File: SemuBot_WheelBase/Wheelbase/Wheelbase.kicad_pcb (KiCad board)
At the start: 2 copper layers, 110 x 90 mm, 136 parts, among them IC1 DRV8353FSRTAR, IC2 DRV8353FSRTAR, IC3 DRV8353FSRTAR, IC4 ADS131M03IRUKT, IC5 ADS131M03IRUKT, IC6 ADS131M03IRUKT, J1 10155435-00011LF, J10 B5B-XH-A_LF__SN_, J11 B5B-XH-A_LF__SN_, J12 B5B-XH-A_LF__SN_, J13 MTSW-104-09-L-S-400, J14 XT30PW-M, J15 MTSW-104-09-L-S-400, J2 MTSW-102-09-L-S-400, J3 MR30PW-M, J4 B5B-XH-A_LF__SN_, J5 B5B-XH-A_LF__SN_, J6 B5B-XH-A_LF__SN_, J7 MR30PW-M, J8 MR30PW-M, J9 DS1013-10SSIB1, Q1 AON7262E, Q10 AON7262E, Q11 AON7262E, Q12 AON7262E, Q13 AON7262E, Q14 AON7262E, Q15 AON7262E, Q19 AON7262E, Q2 AON7262E, Q20 AON7262E, Q21 AON7262E, Q3 AON7262E, Q4 AON7262E, Q5 AON7262E, Q6 AON7262E, Q7 AON7262E, Q8 AON7262E, Q9 AON7262E, U1 STM32F303RET6, U5 RT9013-33GB, Y1 ECS-2520MVLC-081.92-CN-TR, Y2 X322516MLB4SI

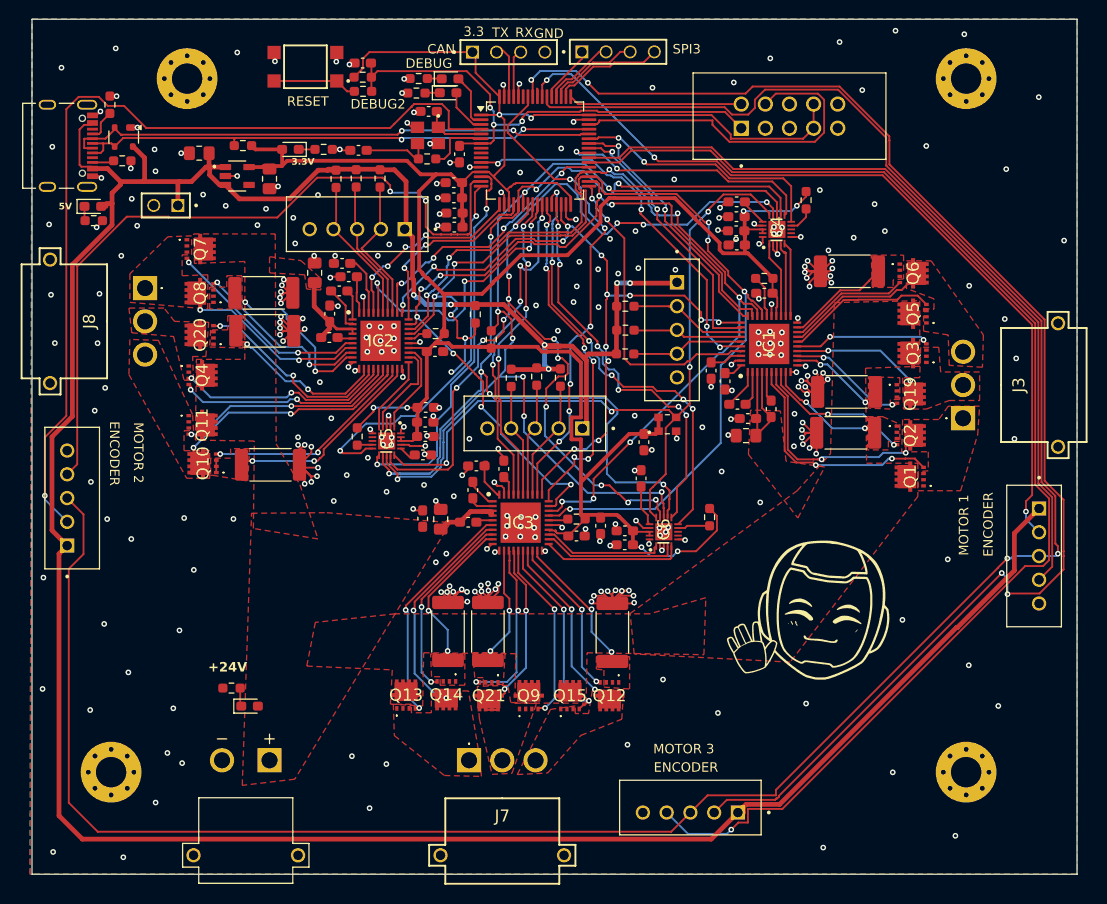
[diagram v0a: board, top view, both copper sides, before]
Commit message: New 4-layer board
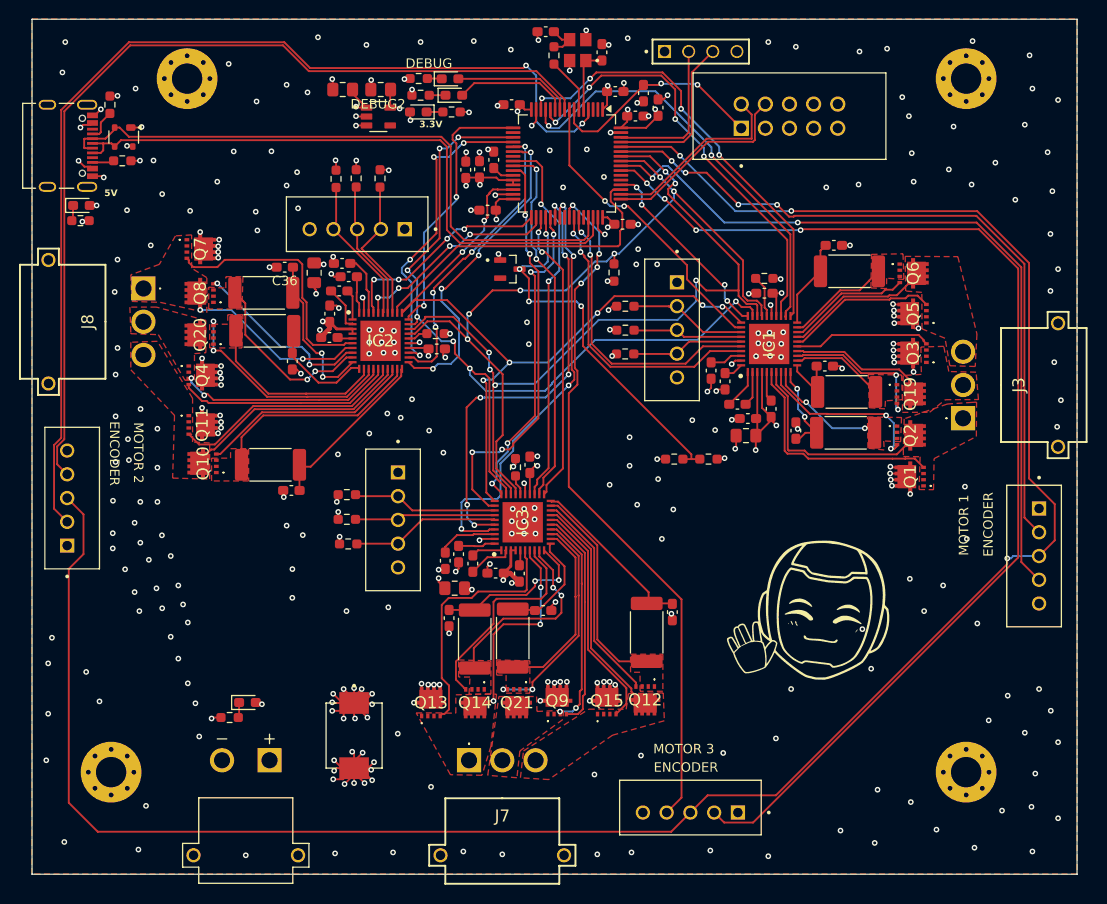
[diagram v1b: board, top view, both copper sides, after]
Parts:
- removed C2, C50, C51, C52, C53: 100nF, Capacitor_SMD:C_0603_1608Metric_Pad1.08x0.95mm_HandSolder
- removed C22: 220nF, Capacitor_SMD:C_0603_1608Metric_Pad1.08x0.95mm_HandSolder
- removed IC4, IC5, IC6: ADS131M03IRUKT, ADS131M:QFN40P300X300X80-21N-D
- removed J15: MTSW-104-09-L-S-400, MTSW-104-09-L-S-400:SAMTEC_MTSW-104-09-L-S-400
- removed J2: MTSW-102-09-L-S-400, MTSW-102-09-L-S-400.:SAMTEC_MTSW-102-09-L-S-400
- removed R21, R22, R3: 1.5K, Resistor_SMD:R_0603_1608Metric_Pad0.98x0.95mm_HandSolder
- removed R23: 10k, Resistor_SMD:R_0603_1608Metric_Pad0.98x0.95mm_HandSolder
- removed R24: 100, Resistor_SMD:R_0603_1608Metric_Pad0.98x0.95mm_HandSolder
- removed R36: 1.5k, Resistor_SMD:R_0603_1608Metric_Pad0.98x0.95mm_HandSolder
- removed S1: SWT0211-050010GSA_REVA, switch:SW_SWT0211-050010GSA_REVA
- removed Y1: ECS-2520MVLC-081.92-CN-TR, ECS-2520:OSC_ECS-2520MVLC-081.92-CN-TR
- added C41: 1uF 63V, Capacitor_SMD:C_0603_1608Metric_Pad1.08x0.95mm_HandSolder, F.Cu at (185.1, 97.3)
- added C42: 1uF 63V, Capacitor_SMD:C_0603_1608Metric_Pad1.08x0.95mm_HandSolder, F.Cu at (129.1, 96.8)
- added C43: 1uF 63V, Capacitor_SMD:C_0603_1608Metric_Pad1.08x0.95mm_HandSolder, F.Cu at (155.5, 123.0)
- added C44: 100nF, Capacitor_SMD:C_0603_1608Metric_Pad1.08x0.95mm_HandSolder, F.Cu at (165.2, 70.9)
- added C45: 100nF, Capacitor_SMD:C_0603_1608Metric_Pad1.08x0.95mm_HandSolder, F.Cu at (148.8, 76.5)
- added C46: 100nF, Capacitor_SMD:C_0603_1608Metric_Pad1.08x0.95mm_HandSolder, F.Cu at (147.3, 76.6)
- added D4: BZX84C3V3, BZX84C3V3:SOT95P240X115-3N, F.Cu at (152.0, 87.0)
- added D5: SMCJ33A, SMCJ33A:DIOM6859X262N, F.Cu at (135.6, 136.2)
- added R27: 10k, Resistor_SMD:R_0603_1608Metric_Pad0.98x0.95mm_HandSolder, F.Cu at (169.3, 107.0)
- C16, C34: value 220nF -> 100nF
- C35, C36, C37, C38, C39, C40: value 100nF -> 1uF 63V
- Q1, Q10, Q11, Q12, Q13, Q14, Q15, Q19, Q2, Q20, Q21, Q3, Q4, Q5, Q6, Q7, Q8, Q9: value AON7262E -> AONR62818
- R26: value 3.3K -> 91k
- U1: value STM32F303RET6 -> STM32G474RET6
- moved C34 36.9 mm to (150.3, 75.5), turned to 90 degrees
- moved R26 26.1 mm to (172.9, 107.0), turned to 180 degrees
- moved R31 25.6 mm to (134.8, 110.8), turned to 180 degrees
- moved R34 25.0 mm to (134.8, 113.4), turned to 180 degrees
- moved R38 24.5 mm to (135.0, 116.0), turned to 180 degrees
- moved C10 23.3 mm to (155.7, 62.1)
- moved C36 23.2 mm to (128.3, 86.8), turned to 180 degrees
- moved C35 20.5 mm to (182.1, 104.0), turned to 90 degrees
- moved C3 20.4 mm to (166.0, 68.5)
- moved J13 20.2 mm to (172.1, 64.2)
- moved C15 19.5 mm to (163.1, 68.4), turned to 0 degrees
- moved C11 19.3 mm to (161.7, 64.2), turned to 90 degrees
- moved C37 18.7 mm to (145.6, 123.8)
- moved Y2 18.1 mm to (159.1, 64.0), turned to 180 degrees
- moved J6 18.1 mm to (139.7, 113.5), turned to 90 degrees
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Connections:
- C16 pad 1: GND -> +3.3V
- C16 pad 2: Net-(IC4-CAP) -> GND
- C34 pad 1: GND -> Net-(U1-VSSA)
- C34 pad 2: Net-(IC6-CAP) -> GND
- C35 pad 1: +3.3V -> /Motor_1/SNA
- C36 pad 1: +3.3V -> /Motor_2/SNA
- C37 pad 1: +3.3V -> /Motor_3/SNA
- C38 pad 1: +3.3V -> /Motor_1/SNC
- C39 pad 1: +3.3V -> /Motor_2/SNC
- C40 pad 1: +3.3V -> /Motor_3/SNC
- IC1 pad 10: GND -> /Motor_1/SNA
- IC1 pad 11: GND -> /Motor_1/SNB
- IC1 pad 20: GND -> /Motor_1/SNC
- IC1 pad 21: /Motor_1/SOC -> /ADC1_IN3
- IC1 pad 22: /Motor_1/SOB -> /ADC1_IN2
- IC1 pad 23: /Motor_1/SOA -> /ADC1_IN1
- IC2 pad 10: GND -> /Motor_2/SNA
- IC2 pad 11: GND -> /Motor_2/SNB
- IC2 pad 20: GND -> /Motor_2/SNC
- IC2 pad 21: /Motor_2/SOC -> /ADC2_IN5
- IC2 pad 22: /Motor_2/SOB -> /ADC2_IN4
- IC2 pad 23: /Motor_2/SOA -> /ADC2_IN3
- IC3 pad 10: GND -> /Motor_3/SNA
- IC3 pad 11: GND -> /Motor_3/SNB
- IC3 pad 20: GND -> /Motor_3/SNC
- IC3 pad 21: /Motor_3/SOC -> /ADC3_IN5
- IC3 pad 22: /Motor_3/SOB -> /ADC3_IN1
- IC3 pad 23: /Motor_3/SOA -> /ADC3_IN12
- R10 pad 1: GND -> /Motor_2/SNA
- R11 pad 1: GND -> /Motor_3/SNA
- R12 pad 1: GND -> /Motor_1/SNC
- R13 pad 1: GND -> /Motor_2/SNC
- R14 pad 1: GND -> /Motor_3/SNC
- R15 pad 1: GND -> /Motor_1/SNB
- R16 pad 1: GND -> /Motor_2/SNB
- R17 pad 1: GND -> /Motor_3/SNB
- R26 pad 1: /SPI1_MISO -> +24V
- R26 pad 2: +3.3V -> /ADC4_IN3
- R9 pad 1: GND -> /Motor_1/SNA
- U1 pad 10: unconnected-(U1-PC2-Pad10) -> Net-(D2-A)
- U1 pad 11: /MOTOR1_DIR -> Net-(D1-A)
- U1 pad 12: GND -> /ADC1_IN1
- U1 pad 13: +3.3V -> /ADC1_IN2
- U1 pad 14: /motor2_DRDY -> /ADC1_IN3
- U1 pad 15: /CS_ENC_2 -> GND
- U1 pad 16: /motor2_adc -> +3.3V
- U1 pad 17: /motor2_nBRAKE -> /motor2_Cs
- U1 pad 18: GND -> /SPI3_NSS
- U1 pad 19: +3.3V -> /SPI_CLK
- U1 pad 2: Net-(D2-A) -> unconnected-(U1-PC13-Pad2)
- U1 pad 20: /motor2_Cs -> /ADC2_IN3
- U1 pad 21: /SPI1_SCK -> /ADC2_IN4
- U1 pad 22: /SPI1_MISO -> /ADC2_IN5
- U1 pad 23: /SPI1_MOSI -> unconnected-(U1-PC5-Pad23)
- U1 pad 24: /MOTOR3_DIR -> /ADC3_IN12
- U1 pad 25: /MOTOR2_DIR -> /ADC3_IN1
- U1 pad 26: /motor3_nBRAKE -> /MOTOR3_PWM
- U1 pad 27: /motor3_Cs -> Net-(U1-VSSA)
- U1 pad 28: /motor3_adc -> +3.3V
- U1 pad 29: /motor3_DRDY -> +3.3V
- U1 pad 3: Net-(D1-A) -> unconnected-(U1-PC14-Pad3)
- U1 pad 33: /motor1_nBRAKE -> /motor2_nBRAKE
- U1 pad 34: /SPI_CLK -> /MOTOR2_DIR
- U1 pad 35: /SPI_DATA -> /ADC3_IN5
- U1 pad 36: /SPI_MOSI -> /ADC4_IN3
- U1 pad 37: /MOTOR2_PWM -> /motor3_Cs
- U1 pad 38: /CS_ENC_3 -> /MOTOR3_DIR
- U1 pad 39: /CS_ENC_1 -> /motor3_nBRAKE
- U1 pad 40: /motor1_DRDY -> unconnected-(U1-PC8-Pad40)
- U1 pad 41: /MOTOR1_PWM -> /CS_ENC_3
- U1 pad 42: /motor1_Cs -> /motor1_nBRAKE
- U1 pad 43: /motor1_adc -> /MOTOR1_DIR
- U1 pad 44: /D- -> unconnected-(U1-PA10-Pad44)
- U1 pad 45: /D+ -> /D-
- U1 pad 46: /SWDIO -> /D+
- U1 pad 49: /SWCLK -> /SWDIO
- U1 pad 50: /SPI3_NSS -> /SWCLK
- U1 pad 51: /SPI3_SCK -> /MOTOR2_PWM
- U1 pad 52: /SPI3_MISO -> /motor1_Cs
- U1 pad 53: /SPI3_MOSI -> unconnected-(U1-PC11-Pad53)
- U1 pad 54: /SSI_CLK -> unconnected-(U1-PC12-Pad54)
- U1 pad 55: /enc_1_data -> /enc_3_data
- U1 pad 56: unconnected-(U1-PB4-Pad56) -> /CS_ENC_1
- U1 pad 57: /enc_3_data -> /SPI_DATA
- U1 pad 58: /MOTOR3_PWM -> /SPI_MOSI
- U1 pad 59: unconnected-(U1-PB7-Pad59) -> /enc_1_data
- U1 pad 60: GND -> /SSI_CLK
- U1 pad 8: unconnected-(U1-PC0-Pad8) -> /MOTOR1_PWM
- U1 pad 9: unconnected-(U1-PC1-Pad9) -> /CS_ENC_2
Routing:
- net +5V: track 318.1 -> 17.7 mm, vias 6 -> 16
- net +3.3V: track 299.8 -> 41.8 mm, vias 8 -> 16
- net GND: track 212.6 -> 89.0 mm, vias 298 -> 270
- net /SPI1_SCK: track 113.6 -> 0.00 mm, vias 7 -> 0
- net /SPI1_MOSI: track 110.1 -> 0.00 mm, vias 15 -> 0
- net /SPI1_MISO: track 105.2 -> 0.00 mm, vias 8 -> 0
- net /adc_CLK: track 78.9 -> 0.00 mm, vias 4 -> 0
- net /CS_ENC_3: track 134.6 -> 73.6 mm, vias 1 -> 4
- net /motor3_adc: track 47.1 -> 0.00 mm, vias 6 -> 0
- net +24V: track 31.9 -> 78.6 mm, vias 0 -> 66
- net /ADC1_IN3: track 0.00 -> 46.5 mm, vias 0 -> 4
- net /ADC1_IN1: track 0.00 -> 45.9 mm, vias 0 -> 4
- net /ADC1_IN2: track 0.00 -> 44.6 mm, vias 0 -> 2
- net /motor3_DRDY: track 42.5 -> 0.00 mm, vias 6 -> 0
- net /motor2_DRDY: track 40.7 -> 0.00 mm, vias 2 -> 0
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- added copper zone on In2.Cu, net +24V
- added copper zone on In2.Cu, net +3.3V
- added copper zone on In2.Cu, net +5V
- added copper zone on In1.Cu, net GND
- removed copper zone on F.Cu, net +24V
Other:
- copper layers 2 -> 4
- board text removed: "+24V"
- board text removed: "3.3"
- board text removed: "CAN"
- board text removed: "GND"
- board text removed: "RESET"
- board text removed: "RX"
- board text removed: "SPI3"
- board text removed: "TX"

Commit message: Fixes
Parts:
- removed R4, R7, R8: 3.3K, Resistor_SMD:R_0603_1608Metric_Pad0.98x0.95mm_HandSolder
- added C47: 100nF, Capacitor_SMD:C_0603_1608Metric_Pad1.08x0.95mm_HandSolder, F.Cu at (110.9, 116.2)
- added C48: 100nF, Capacitor_SMD:C_0603_1608Metric_Pad1.08x0.95mm_HandSolder, F.Cu at (176.3, 139.2)
- added C49: 100nF, Capacitor_SMD:C_0603_1608Metric_Pad1.08x0.95mm_HandSolder, F.Cu at (202.4, 111.7)
- added C50: 470uF 5mm 63V Polymer, Capacitor_THT:CP_Radial_D10.0mm_P5.00mm, F.Cu at (130.7, 119.3)
- added C51: 470uF 5mm 63V Polymer, Capacitor_THT:CP_Radial_D10.0mm_P5.00mm, F.Cu at (114.8, 121.5)
- added C52: 470uF 5mm 63V Polymer, Capacitor_THT:CP_Radial_D10.0mm_P5.00mm, F.Cu at (122.1, 131.1)
- added C53: 100nF, Capacitor_SMD:C_0603_1608Metric_Pad1.08x0.95mm_HandSolder, F.Cu at (136.0, 123.3)
- C35, C36, C37, C38, C39, C40, C41, C42, C43: value 1uF 63V -> 1uF 50V X7R; footprint Capacitor_SMD:C_0603_1608Metric_Pad1.08x0.95mm_HandSolder -> Capacitor_SMD:C_0805_2012Metric_Pad1.18x1.45mm_HandSolder
- moved C39 62.7 mm to (189.8, 95.5)
- moved C42 62.2 mm to (190.0, 109.5)
- moved C36 61.8 mm to (189.9, 91.8)
- moved C38 51.8 mm to (157.9, 128.0), turned to 90 degrees
- moved C40 51.5 mm to (124.3, 97.8), turned to 0 degrees
- moved C43 50.7 mm to (123.2, 83.8), turned to 90 degrees
- moved C35 46.9 mm to (142.3, 128.8), turned to 180 degrees
- moved C41 38.9 mm to (161.7, 128.3), turned to 90 degrees
- moved C37 31.8 mm to (123.3, 101.0), turned to 90 degrees
- moved R18 18.8 mm to (141.2, 136.1), turned to -90 degrees
- moved D7 15.3 mm to (139.6, 134.2), turned to 90 degrees
- moved C10 2.21 mm to (154.8, 64.0), turned to 90 degrees
- moved R5 0.35 mm to (156.3, 64.7)
- moved Y2 0.35 mm to (159.1, 64.3)
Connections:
- C35 pad 1: /Motor_1/SNA -> +24V
- C36 pad 1: /Motor_2/SNA -> +24V
- C37 pad 1: /Motor_3/SNA -> +24V
- C38 pad 1: /Motor_1/SNC -> +24V
- C39 pad 1: /Motor_2/SNC -> +24V
- C40 pad 1: /Motor_3/SNC -> +24V
- C41 pad 1: /Motor_1/SNB -> +24V
- C42 pad 1: /Motor_2/SNB -> +24V
- C43 pad 1: /Motor_3/SNB -> +24V
- IC1 pad 10: /Motor_1/SNA -> GND
- IC1 pad 11: /Motor_1/SNB -> GND
- IC1 pad 20: /Motor_1/SNC -> GND
- IC1 pad 26: Net-(IC1-NFAULT) -> unconnected-(IC1-NFAULT-Pad26)
- IC2 pad 10: /Motor_2/SNA -> GND
- IC2 pad 11: /Motor_2/SNB -> GND
- IC2 pad 20: /Motor_2/SNC -> GND
- IC2 pad 26: Net-(IC2-NFAULT) -> unconnected-(IC2-NFAULT-Pad26)
- IC3 pad 10: /Motor_3/SNA -> GND
- IC3 pad 11: /Motor_3/SNB -> GND
- IC3 pad 20: /Motor_3/SNC -> GND
- IC3 pad 26: Net-(IC3-NFAULT) -> unconnected-(IC3-NFAULT-Pad26)
- R10 pad 1: /Motor_2/SNA -> GND
- R11 pad 1: /Motor_3/SNA -> GND
- R12 pad 1: /Motor_1/SNC -> GND
- R13 pad 1: /Motor_2/SNC -> GND
- R14 pad 1: /Motor_3/SNC -> GND
- R15 pad 1: /Motor_1/SNB -> GND
- R16 pad 1: /Motor_2/SNB -> GND
- R17 pad 1: /Motor_3/SNB -> GND
- R9 pad 1: /Motor_1/SNA -> GND
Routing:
- net GND: track 89.0 -> 250.4 mm, vias 270 -> 354
- net +24V: track 78.6 -> 112.4 mm, vias 66 -> 67
- net /Motor_2/SNC: track 18.2 -> 0.00 mm
- net /Motor_3/SNC: track 18.2 -> 0.00 mm
- net /Motor_3/SNA: track 17.0 -> 0.00 mm, vias 2 -> 0
- net /Motor_2/SNA: track 17.0 -> 0.00 mm, vias 2 -> 0
- net +5V: track 17.7 -> 31.4 mm, vias 16 -> 18
- net /Motor_2/SNB: track 12.0 -> 0.00 mm
- net /Motor_3/SNB: track 12.0 -> 0.00 mm
- net /Motor_1/SNC: track 9.99 -> 0.00 mm
- net /Motor_1/SNA: track 9.65 -> 0.00 mm, vias 2 -> 0
- net /Motor_1/SNB: track 6.45 -> 0.00 mm
- net Net-(IC1-NFAULT): track 4.44 -> 0.00 mm
- net /Motor_3/SPA: track 20.5 -> 17.4 mm, vias 2 -> 0
- net +3.3V: track 41.8 -> 39.3 mm, vias 16 -> 13
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- added copper zone on In2.Cu, net GND
